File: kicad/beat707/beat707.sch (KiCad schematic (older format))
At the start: 5 parts, among them J1 USB_B, J2 DIN-5_180degree, J3 AudioJack3_Ground, J4 DIN-5_180degree, U1 ATmega328-PU

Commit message: 3 new buttons and a rotary encoder (ALPS EC12E)
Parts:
- added SW25, SW26, SW27: SW_Push, beat707:K2-1103SP-A4SW-04, symbol switch:SW_Push
- added SW28: Rotary_Encoder, Rotary_Encoder:RotaryEncoder_Alps_EC12E_Vertical_H20mm, symbol Device:Rotary_Encoder
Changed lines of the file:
@@
 EESchema Schematic File Version 4
+LIBS:beat707-cache
 EELAYER 26 0
 EELAYER END
@@
 	1    0    0    -1
 $EndComp
+$Comp
+L switch:SW_Push SW?
+U 1 1 5C74CDB9
+P 3350 2650
+AR Path="/5C65184E/5C74CDB9" Ref="SW?"  Part="1"
+AR Path="/5C6557AC/5C74CDB9" Ref="SW?"  Part="1"
+AR Path="/5C6559D3/5C74CDB9" Ref="SW?"  Part="1"
+AR Path="/5C74CDB9" Ref="SW25"  Part="1"
+F 0 "SW25" H 3350 2935 50  0000 C CNN
+F 1 "SW_Push" H 3350 2844 50  0000 C CNN
+F 2 "beat707:K2-1103SP-A4SW-04" H 3350 2850 50  0001 C CNN
+F 3 "" H 3350 2850 50  0001 C CNN
+	1    3350 2650
+	1    0    0    -1
+$EndComp
+$Comp
+L switch:SW_Push SW?
+U 1 1 5C74CDF8
+P 3350 3200
+AR Path="/5C65184E/5C74CDF8" Ref="SW?"  Part="1"
+AR Path="/5C6557AC/5C74CDF8" Ref="SW?"  Part="1"
+AR Path="/5C6559D3/5C74CDF8" Ref="SW?"  Part="1"
+AR Path="/5C74CDF8" Ref="SW26"  Part="1"
+F 0 "SW26" H 3350 3485 50  0000 C CNN
+F 1 "SW_Push" H 3350 3394 50  0000 C CNN
+F 2 "beat707:K2-1103SP-A4SW-04" H 3350 3400 50  0001 C CNN
+F 3 "" H 3350 3400 50  0001 C CNN
+	1    3350 3200
+	1    0    0    -1
+$EndComp
+$Comp
+L switch:SW_Push SW?
+U 1 1 5C74CE2B
+P 3400 3750
+AR Path="/5C65184E/5C74CE2B" Ref="SW?"  Part="1"
+AR Path="/5C6557AC/5C74CE2B" Ref="SW?"  Part="1"
+AR Path="/5C6559D3/5C74CE2B" Ref="SW?"  Part="1"
+AR Path="/5C74CE2B" Ref="SW27"  Part="1"
+F 0 "SW27" H 3400 4035 50  0000 C CNN
+F 1 "SW_Push" H 3400 3944 50  0000 C CNN
+F 2 "beat707:K2-1103SP-A4SW-04" H 3400 3950 50  0001 C CNN
+F 3 "" H 3400 3950 50  0001 C CNN
+	1    3400 3750
+	1    0    0    -1
+$EndComp
+$Comp
+L Device:Rotary_Encoder SW28
+U 1 1 5C74D2CA
+P 7000 3750
+F 0 "SW28" H 7229 3796 50  0000 L CNN
+F 1 "Rotary_Encoder" H 7229 3705 50  0000 L CNN
+F 2 "Rotary_Encoder:RotaryEncoder_Alps_EC12E_Vertical_H20mm" H 6850 3910 50  0001 C CNN
+F 3 "~" H 7000 4010 50  0001 C CNN
+	1    7000 3750
+	1    0    0    -1
+$EndComp

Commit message: more LEDs, switches and resistors for version encoding
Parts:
- removed SW28: Rotary_Encoder, Rotary_Encoder:RotaryEncoder_Alps_EC12E_Vertical_H20mm, symbol Device:Rotary_Encoder
- added SW4: Rotary_Encoder_Switch, Rotary_Encoder:RotaryEncoder_Alps_EC11E-Switch_Vertical_H20mm, symbol Device:Rotary_Encoder_Switch
- renumbered J3 to J2, J2 to J3, SW25 to SW1, SW26 to SW2, SW27 to SW3
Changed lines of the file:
@@
 $EndComp
 $Comp
-L Connector:AudioJack3_Ground J3
+L Connector:AudioJack3_Ground J2
 U 1 1 5C6560D3
 P 8000 5150
-F 0 "J3" H 8004 5492 50  0000 C CNN
+F 0 "J2" H 8004 5492 50  0000 C CNN
 F 1 "AudioJack3_Ground" H 8004 5401 50  0000 C CNN
 F 2 "Connector_Audio:Jack_3.5mm_PJ311_Horizontal" H 8000 5150 50  0001 C CNN
@@
 $EndComp
 $Comp
-L Connector:DIN-5_180degree J2
+L Connector:DIN-5_180degree J3
 U 1 1 5C65661A
 P 8550 2800
-F 0 "J2" H 8550 2526 50  0000 C CNN
+F 0 "J3" H 8550 2526 50  0000 C CNN
 F 1 "DIN-5_180degree" H 8550 2435 50  0000 C CNN
 F 2 "beat707:DIN-Socket" H 8550 2800 50  0001 C CNN
@@
 AR Path="/5C6557AC/5C74CDB9" Ref="SW?"  Part="1"
 AR Path="/5C6559D3/5C74CDB9" Ref="SW?"  Part="1"
-AR Path="/5C74CDB9" Ref="SW25"  Part="1"
-F 0 "SW25" H 3350 2935 50  0000 C CNN
+AR Path="/5C74CDB9" Ref="SW1"  Part="1"
+F 0 "SW1" H 3350 2935 50  0000 C CNN
 F 1 "SW_Push" H 3350 2844 50  0000 C CNN
 F 2 "beat707:K2-1103SP-A4SW-04" H 3350 2850 50  0001 C CNN
@@
 AR Path="/5C6557AC/5C74CDF8" Ref="SW?"  Part="1"
 AR Path="/5C6559D3/5C74CDF8" Ref="SW?"  Part="1"
-AR Path="/5C74CDF8" Ref="SW26"  Part="1"
-F 0 "SW26" H 3350 3485 50  0000 C CNN
+AR Path="/5C74CDF8" Ref="SW2"  Part="1"
+F 0 "SW2" H 3350 3485 50  0000 C CNN
 F 1 "SW_Push" H 3350 3394 50  0000 C CNN
 F 2 "beat707:K2-1103SP-A4SW-04" H 3350 3400 50  0001 C CNN
@@
 AR Path="/5C6557AC/5C74CE2B" Ref="SW?"  Part="1"
 AR Path="/5C6559D3/5C74CE2B" Ref="SW?"  Part="1"
-AR Path="/5C74CE2B" Ref="SW27"  Part="1"
-F 0 "SW27" H 3400 4035 50  0000 C CNN
+AR Path="/5C74CE2B" Ref="SW3"  Part="1"
+F 0 "SW3" H 3400 4035 50  0000 C CNN
 F 1 "SW_Push" H 3400 3944 50  0000 C CNN
 F 2 "beat707:K2-1103SP-A4SW-04" H 3400 3950 50  0001 C CNN
@@
 $EndComp
 $Comp
-L Device:Rotary_Encoder SW28
-U 1 1 5C74D2CA
-P 7000 3750
-F 0 "SW28" H 7229 3796 50  0000 L CNN
-F 1 "Rotary_Encoder" H 7229 3705 50  0000 L CNN
-F 2 "Rotary_Encoder:RotaryEncoder_Alps_EC12E_Vertical_H20mm" H 6850 3910 50  0001 C CNN
-F 3 "~" H 7000 4010 50  0001 C CNN
-	1    7000 3750
+L Device:Rotary_Encoder_Switch SW4
+U 1 1 5C812DB9
+P 7000 3900
+F 0 "SW4" H 7000 4267 50  0000 C CNN
+F 1 "Rotary_Encoder_Switch" H 7000 4176 50  0000 C CNN
+F 2 "Rotary_Encoder:RotaryEncoder_Alps_EC11E-Switch_Vertical_H20mm" H 6850 4060 50  0001 C CNN
+F 3 "~" H 7000 4160 50  0001 C CNN
+	1    7000 3900
 	1    0    0    -1
 $EndComp

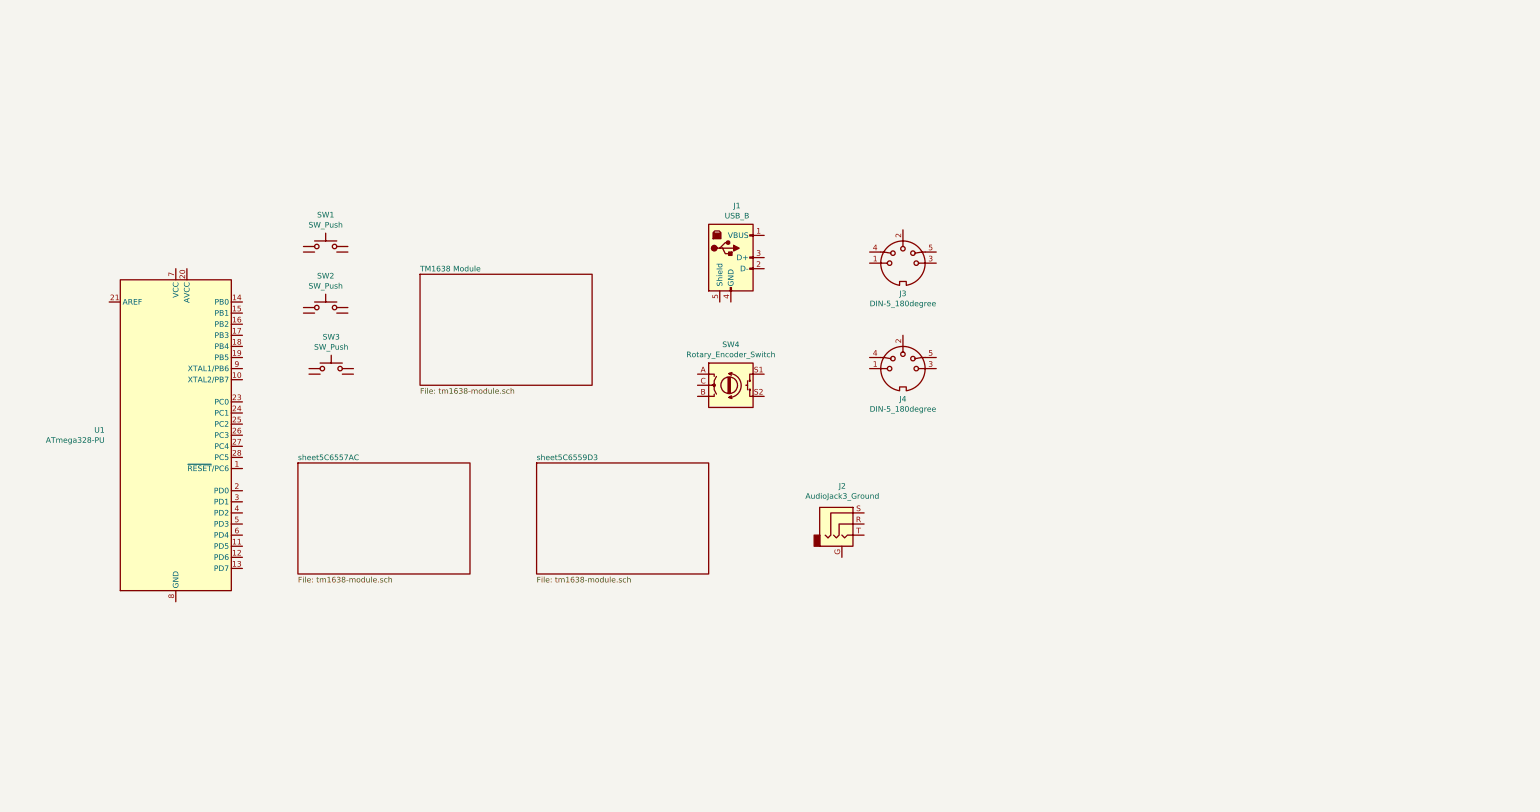
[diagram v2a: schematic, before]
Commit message: test board for TM1638 and main board finished
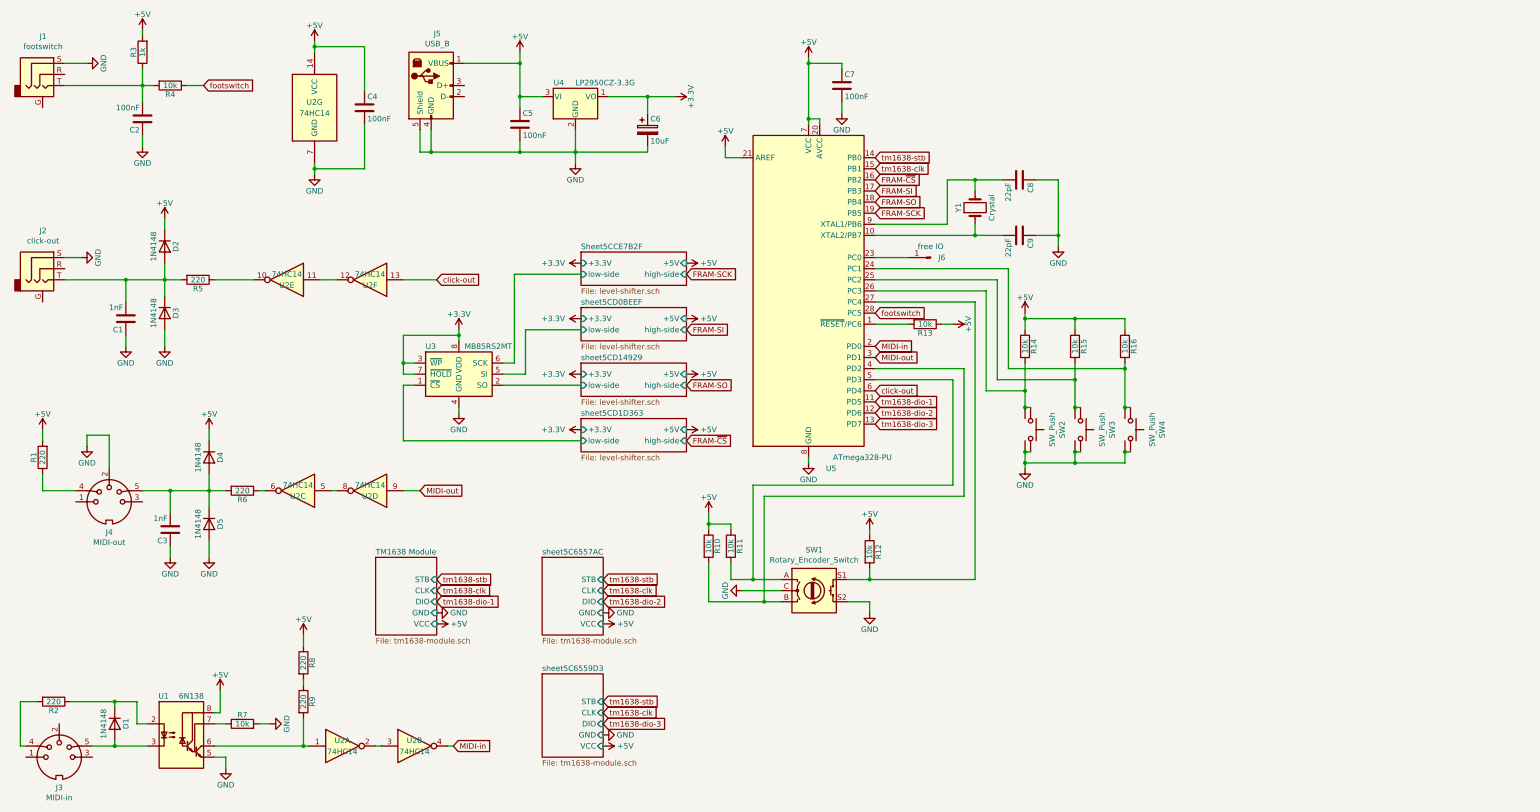
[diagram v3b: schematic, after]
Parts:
- added C1, C3: 1nF, Capacitor_THT:C_Disc_D3.0mm_W2.0mm_P2.50mm, symbol Device:C
- added C2, C4, C5, C7: 100nF, Capacitor_THT:C_Disc_D3.0mm_W2.0mm_P2.50mm, symbol Device:C
- added C6: 10uF, Capacitor_THT:CP_Radial_D6.3mm_P2.50mm, symbol Device:CP
- added C8, C9: 22pF, Capacitor_THT:C_Disc_D3.0mm_W2.0mm_P2.50mm, symbol Device:C
- added D1, D2, D3, D4, D5: 1N4148, Diode_THT:D_DO-35_SOD27_P7.62mm_Horizontal, symbol Diode:1N4148
- added J1: footswitch, Connector_Audio:Jack_3.5mm_PJ311_Horizontal, symbol Connector:AudioJack3_Ground
- added J6: free IO, symbol Connector:Conn_01x01_Male
- added R1, R2, R5, R6, R8, R9: 220, Resistor_THT:R_Axial_DIN0207_L6.3mm_D2.5mm_P7.62mm_Horizontal, symbol Device:R
- added R10, R11, R12, R13, R14, R15, R16, R4, R7: 10k, Resistor_THT:R_Axial_DIN0207_L6.3mm_D2.5mm_P7.62mm_Horizontal, symbol Device:R
- added R3: 1k, Resistor_THT:R_Axial_DIN0207_L6.3mm_D2.5mm_P7.62mm_Horizontal, symbol Device:R
- added U1: 6N138, Package_DIP:DIP-8_W7.62mm, symbol Isolator:6N138
- added U2: 74HC14, Package_DIP:DIP-14_W7.62mm, symbol 74xx:74HC14
- added U3: MB85RS2MT, beat707:trs, symbol Memory_NVRAM:MB85RS2MT
- added U4: LP2950CZ-3.3G, Package_TO_SOT_THT:TO-92_Inline, symbol Regulator_Linear:LM78L05_TO92
- added Y1: Crystal, Crystal:Crystal_HC49-U_Vertical, symbol Device:Crystal
- J2: value AudioJack3_Ground -> click-out
- J3: renamed from J4; value DIN-5_180degree -> MIDI-in; footprint beat707:DIN-Socket -> beat707:din-5
- J4: renamed from J3; value DIN-5_180degree -> MIDI-out; footprint beat707:DIN-Socket -> beat707:din-5
- SW2: renamed from SW1; footprint beat707:K2-1103SP-A4SW-04 -> beat707:B3F-through-hole
- SW3: renamed from SW2; footprint beat707:K2-1103SP-A4SW-04 -> beat707:B3F-through-hole
- SW4: renamed from SW3; footprint beat707:K2-1103SP-A4SW-04 -> beat707:B3F-through-hole
- renumbered J1 to J5, SW4 to SW1, U1 to U5
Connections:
- net at U5.1 (~RESET~/PC6): now also R13.2
- net at U5.10 (XTAL2/PB7): now also C9.2, Y1.1
- net tm1638-dio-1: now reaches U5.11 (PD5)
- net tm1638-dio-2: now reaches U5.12 (PD6)
- net tm1638-dio-3: now reaches U5.13 (PD7)
- net tm1638-stb: now reaches U5.14 (PB0)
- net tm1638-clk: now reaches U5.15 (PB1)
- net FRAM-~CS: now reaches U5.16 (PB2)
- net FRAM-SI: now reaches U5.17 (PB3)
- net FRAM-SO: now reaches U5.18 (PB4)
- net FRAM-SCK: now reaches U5.19 (PB5)
- net MIDI-in: now reaches U5.2 (PD0)
- net MIDI-in: now also U2.4
- net +5V: now reaches U5.20 (AVCC)
- net +5V: now also J5.1 (VBUS), U5.21 (AREF), U5.7 (VCC), C4.1, C5.1, C7.1, D2.1 (K), D4.1 (K), R1.2, R10.1, R11.1, R12.1, R13.1, R14.1, R15.1, R16.1, R3.2, R8.1, U1.8 (VCC), U2.14 (VCC), U4.3 (VI)
- net GND: now reaches U5.22 (GND), U5.8 (GND)
- net GND: now also J2.S, J4.2, J5.4 (GND), J5.5 (Shield), SW1.C, SW1.S2, SW2.3, SW2.4, SW3.3, SW3.4, SW4.3, SW4.4, C1.1, C2.1, C3.1, C4.2, C5.2, C6.2, C7.2, C8.1, C9.1, D3.2 (A), D5.2 (A), J1.S, R7.2, U1.5 (GND), U2.7 (GND), U3.4 (GND), U4.2 (GND)
- net at U5.23 (PC0): now also J6.1 (Pin_1)
- net at U5.24 (PC1): now also SW4.1, SW4.2, R16.2
- net at U5.25 (PC2): now also SW3.1, SW3.2, R15.2
- net at U5.26 (PC3): now also SW2.1, SW2.2, R14.2
- net at U5.27 (PC4): now also SW1.S1, R12.2
- net footswitch: now reaches U5.28 (PC5)
- net footswitch: now also R4.1
- net MIDI-out: now reaches U5.3 (PD1)
- net MIDI-out: now also U2.9
- net at U5.4 (PD2): now also SW1.B, R10.2
- net at U5.5 (PD3): now also SW1.A, R11.2
- net click-out: now reaches U5.6 (PD4)
- net click-out: now also U2.13
- net at U5.9 (XTAL1/PB6): now also C8.2, Y1.2
- net at J2.T: now also C1.2, D2.2 (A), D3.1 (K), R5.2
- net at J4.4: now also R1.1
- net at J4.5: now also C3.2, D4.2 (A), D5.1 (K), R6.2
- net at J3.4: now also R2.2
- net at J3.5: now also D1.2 (A), U1.3 (C2)
- new net: D1.1 (K), R2.1, U1.2 (C1)
- new net: R9.2, U1.6 (VO2), U2.1
- new net: R7.1, U1.7 (VO1)
- new net: U2.2, U2.3
- new net: U2.5, U2.8
- new net: R6.1, U2.6
- new net: R5.1, U2.10
- new net: U2.11, U2.12
- new net: R8.2, R9.1
- new net: C2.2, J1.T, R3.1, R4.2
- new net +3V3: C6.1, U3.3 (~WP), U3.7 (~HOLD), U3.8 (VDD), U4.1 (VO)
- new net Sheet5CCE7B2F/low-side: U3.6 (SCK)
- new net sheet5CD0BEEF/low-side: U3.5 (SI)
- new net sheet5CD14929/low-side: U3.2 (SO)
- new net sheet5CD1D363/low-side: U3.1 (~CS)
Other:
- moved on the sheet: J2, J3, J4, J5, SW1, SW2, SW3, SW4, U5

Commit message: board updated and schematic cleanup
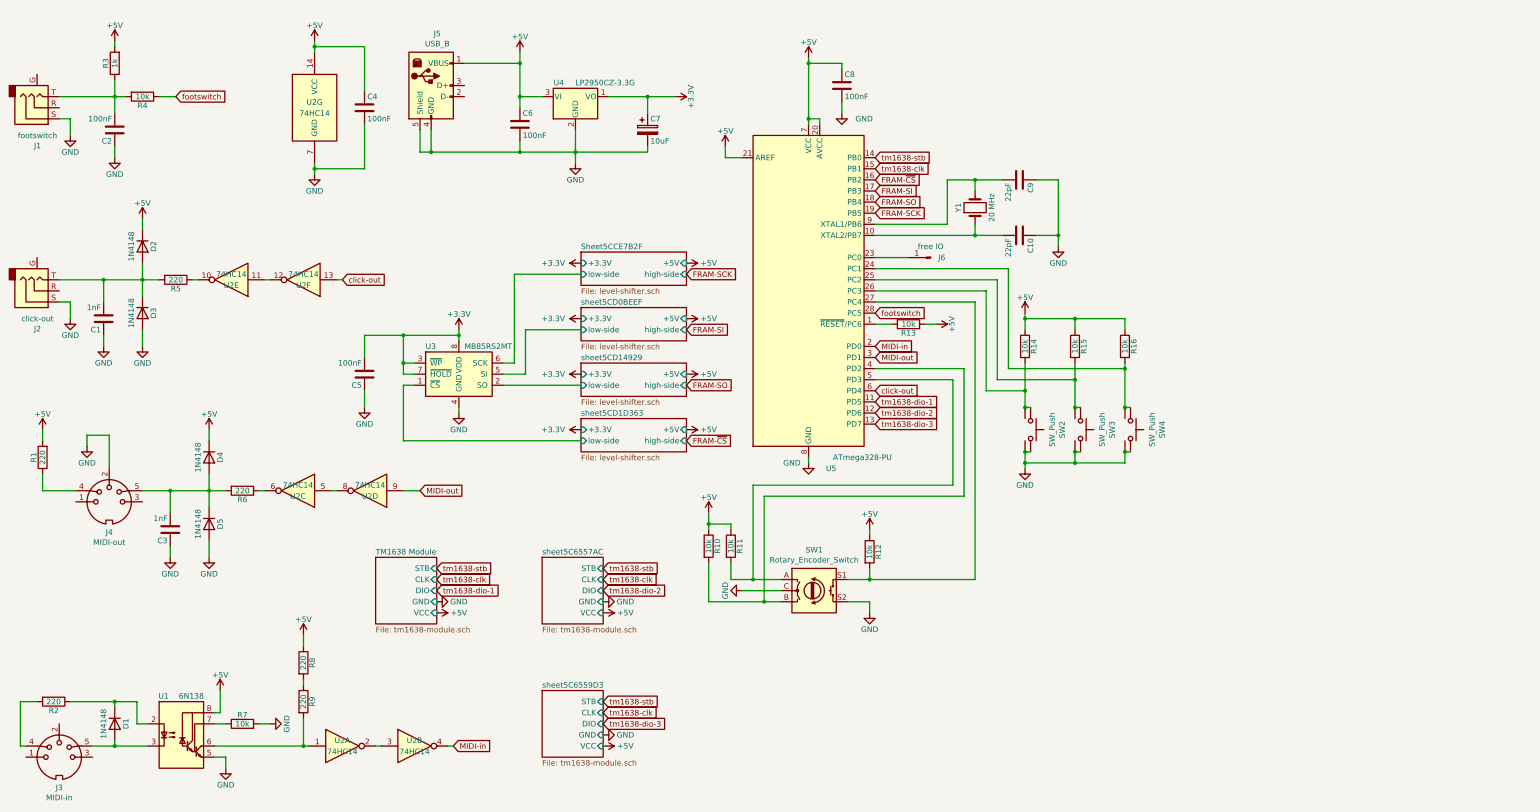
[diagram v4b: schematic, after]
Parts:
- added C5: 100nF, Capacitor_THT:C_Disc_D3.0mm_W2.0mm_P2.50mm, symbol Device:C
- J1, J2: footprint Connector_Audio:Jack_3.5mm_PJ311_Horizontal -> beat707:trs
- U3: footprint beat707:trs -> Package_DIP:DIP-8_W7.62mm
- Y1: value Crystal -> 20 MHz
- renumbered C9 to C10, C5 to C6, C6 to C7, C7 to C8, C8 to C9
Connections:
- net +3V3: now also C5.2
- net GND: now also C5.1
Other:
- moved on the sheet: C1, C2, D2, D3, J1, J2, R13, R3, R4, R5, U2E, U2F

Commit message: restored deleted files and added all 3D models
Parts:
- added Q1: 2N7000, Package_TO_SOT_THT:TO-92_Inline, symbol Transistor_FET:2N7000
- added R119, R121, R124: 2.2k, Resistor_THT:R_Axial_DIN0207_L6.3mm_D2.5mm_P7.62mm_Horizontal, symbol Device:R
- added R120, R122, R123, R125, R126: 3.3k, Resistor_THT:R_Axial_DIN0207_L6.3mm_D2.5mm_P7.62mm_Horizontal, symbol Device:R
- C1, C3: footprint Capacitor_THT:C_Disc_D3.0mm_W2.0mm_P2.50mm -> Capacitor_THT:C_Disc_D8.0mm_W5.0mm_P7.50mm
- J6: footprint (none) -> Connector_PinHeader_2.54mm:PinHeader_1x01_P2.54mm_Vertical
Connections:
- wire segments 198 -> 223
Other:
- moved on the sheet: C1, C5, D2, D3, J2, R5, U2E, U2F, U3

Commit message: new voltage level translation and ISP header
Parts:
- removed C5: 100nF, Capacitor_THT:C_Disc_D3.0mm_W2.0mm_P2.50mm, symbol Device:C
- removed C7: 10uF, Capacitor_THT:CP_Radial_D6.3mm_P2.50mm, symbol Device:CP
- removed Q1: 2N7000, Package_TO_SOT_THT:TO-92_Inline, symbol Transistor_FET:2N7000
- removed R119, R121, R124: 2.2k, Resistor_THT:R_Axial_DIN0207_L6.3mm_D2.5mm_P7.62mm_Horizontal, symbol Device:R
- removed R120, R122, R123, R125, R126: 3.3k, Resistor_THT:R_Axial_DIN0207_L6.3mm_D2.5mm_P7.62mm_Horizontal, symbol Device:R
- removed U3: MB85RS2MT, Package_DIP:DIP-8_W7.62mm, symbol Memory_NVRAM:MB85RS2MT
- removed U4: LP2950CZ-3.3G, Package_TO_SOT_THT:TO-92_Inline, symbol Regulator_Linear:LM78L05_TO92
- added J7: ISP, Connector_PinHeader_2.54mm:PinHeader_2x05_P2.54mm_Vertical, symbol Connector_Generic:Conn_02x05_Odd_Even
- added R127, R128, R129: 1k, Resistor_THT:R_Axial_DIN0207_L6.3mm_D2.5mm_P7.62mm_Horizontal, symbol Device:R
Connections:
- net labels added: MISO, MOSI, RESET, SCK
- net labels removed: +3.3V, FRAM-SCK, FRAM-SI, FRAM-SO, FRAM-~CS
- wire segments 223 -> 188
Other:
- moved on the sheet: C10, C8, C9, J6, R10, R11, R12, R13, R14, R15, R16, SW1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
